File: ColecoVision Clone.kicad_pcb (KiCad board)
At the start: 2 copper layers, 149.4 x 99.1 mm, 141 parts, among them J1 Cartridge Slot, J2 Composite video, J3 PJ-102A, J4 RCJ-017, J5 Controller Port 1, J6 Controller Port 2, Q1 2n4401, Q2 Q_NJFET_GSD, Q3 2N3906, Q4 2N3904, Q5 2N3904, SW1 Power Toggle, SW2 Reset, U1 PLCCZ80, U10 SN76489AN, U11 74LS04, U12 74LS138 (Mem. Mapped), U13 74LS138 (I/O), U14 74LS02, U15 Controller 1, U16 Controller 2, U17 74LS05, U18 74LS05, U2 Work RAM, U20 74LS74, U22 74LS74, U23 74HCT00, U24 TPS60403DBVR, U3 BIOS ROM 27C256, U4 74HCT04, U5 TMS9918A, U6 74LS574, U7 74LS574, U8 74LS574, U9 VRAM, X1 14.31818MHz, Y1 10.738635MHZ

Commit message: U17 now powered
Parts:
- moved U17 0.06 mm to (93.6, 95.9)
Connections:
- U17 pad 14: (no net) -> VCC
- U17 pad 7: (no net) -> GND
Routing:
- net GND: track 1252.8 -> 1259.7 mm
- net VCC: track 926.4 -> 932.7 mm

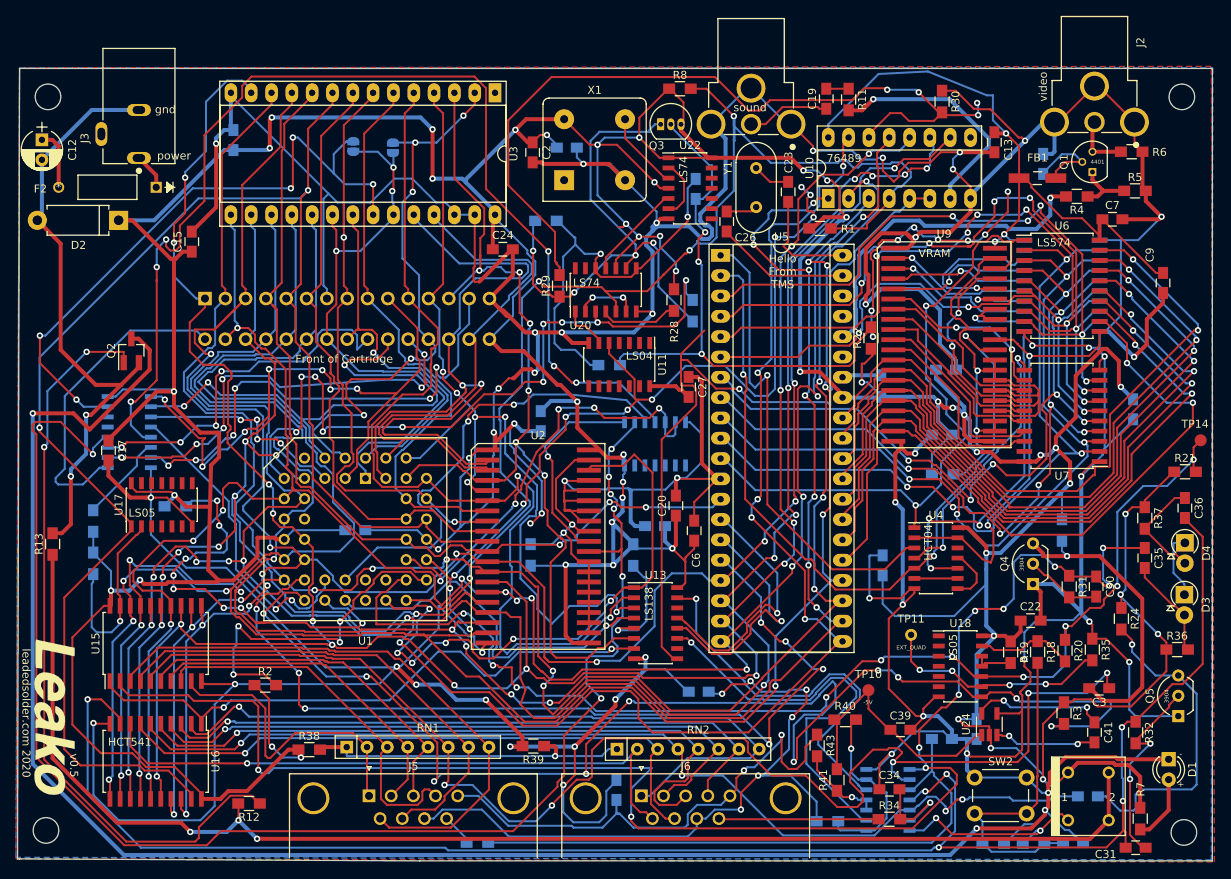
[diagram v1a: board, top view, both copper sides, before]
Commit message: Ground Vpp on the ROM
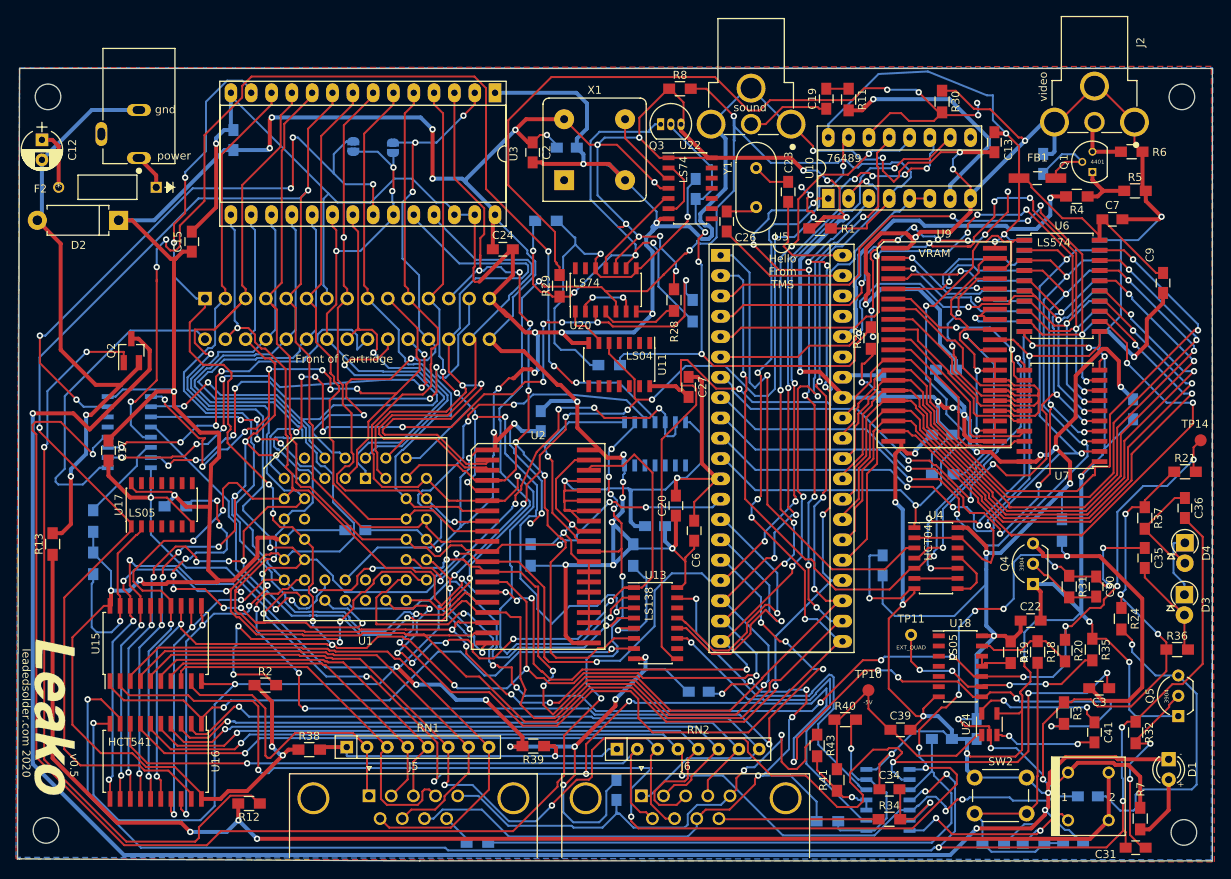
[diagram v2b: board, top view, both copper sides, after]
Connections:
- U3 pad 1: Net-(U3-Pad1) -> GND
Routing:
- net GND: track 1259.7 -> 1277.8 mm
- net CTRL_EN_1: track 51.7 -> 45.8 mm
- net Audio_WR: track 102.0 -> 97.0 mm
- net !INT: track 170.4 -> 166.4 mm
- net CTRL_EN_2: track 50.0 -> 46.2 mm
- net VCC: track 932.7 -> 929.1 mm
- net /Controllers/CTRL_PIN_8: track 86.4 -> 85.5 mm, vias 6 -> 5
- net !RESET: track 149.8 -> 149.2 mm

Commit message: Slowly clearing up vias
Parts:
- moved R30 5.61 mm to (185.8, 43.7), turned to 180 degrees
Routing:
- net GND: track 1277.8 -> 1211.7 mm, vias 55 -> 49
- net !M1: track 107.2 -> 52.6 mm, vias 11 -> 6
- net VCC: track 929.1 -> 907.6 mm
- net AUD_CLK: track 100.5 -> 83.6 mm, vias 4 -> 0
- net A7: track 119.7 -> 113.9 mm, vias 6 -> 4
- net !CART_0x80: track 46.1 -> 43.9 mm
- net /Video/VIDVCC: track 11.0 -> 9.73 mm
- net /Power/CLK_B: track 106.4 -> 105.5 mm, vias 11 -> 10
- net !WAIT: track 150.5 -> 149.8 mm
- net A13: track 76.5 -> 77.2 mm
- net !CART_0xA0: track 55.8 -> 55.3 mm
- net A12: vias 5 -> 4

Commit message: Purging vias
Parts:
- C25, R26: moved to F.Cu
- C34, C41, R32, R36: moved to B.Cu
- moved C25 7.78 mm to (159.3, 64.1), turned to 270 degrees
- moved C34 5.52 mm to (182.7, 126.2)
- moved R26 5.15 mm to (146.7, 61.3)
- moved TP11 5.13 mm to (191.6, 109.5)
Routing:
- net GND: track 1211.7 -> 1238.2 mm, vias 49 -> 48
- net Net-(C32-Pad1): track 129.4 -> 150.7 mm, vias 4 -> 3
- net VCC: track 907.6 -> 886.4 mm, vias 54 -> 49
- net !RD: track 59.0 -> 73.4 mm
- net !CPU_CLK: track 50.9 -> 39.1 mm, vias 2 -> 1
- net Net-(C34-Pad2): track 11.9 -> 19.3 mm
- net /Power/CLK_E: track 68.0 -> 60.9 mm, vias 4 -> 3
- net Net-(C3-Pad1): track 169.3 -> 162.3 mm
- net !WR: track 78.0 -> 74.5 mm
- net D0: track 282.7 -> 279.4 mm
- net Net-(C30-Pad1): track 192.9 -> 189.9 mm
- net A6: track 115.8 -> 112.9 mm
- net /Power/CLK_B: track 105.5 -> 102.8 mm, vias 10 -> 9
- net !WAIT: track 149.8 -> 152.4 mm
- net D6: track 290.3 -> 288.5 mm
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
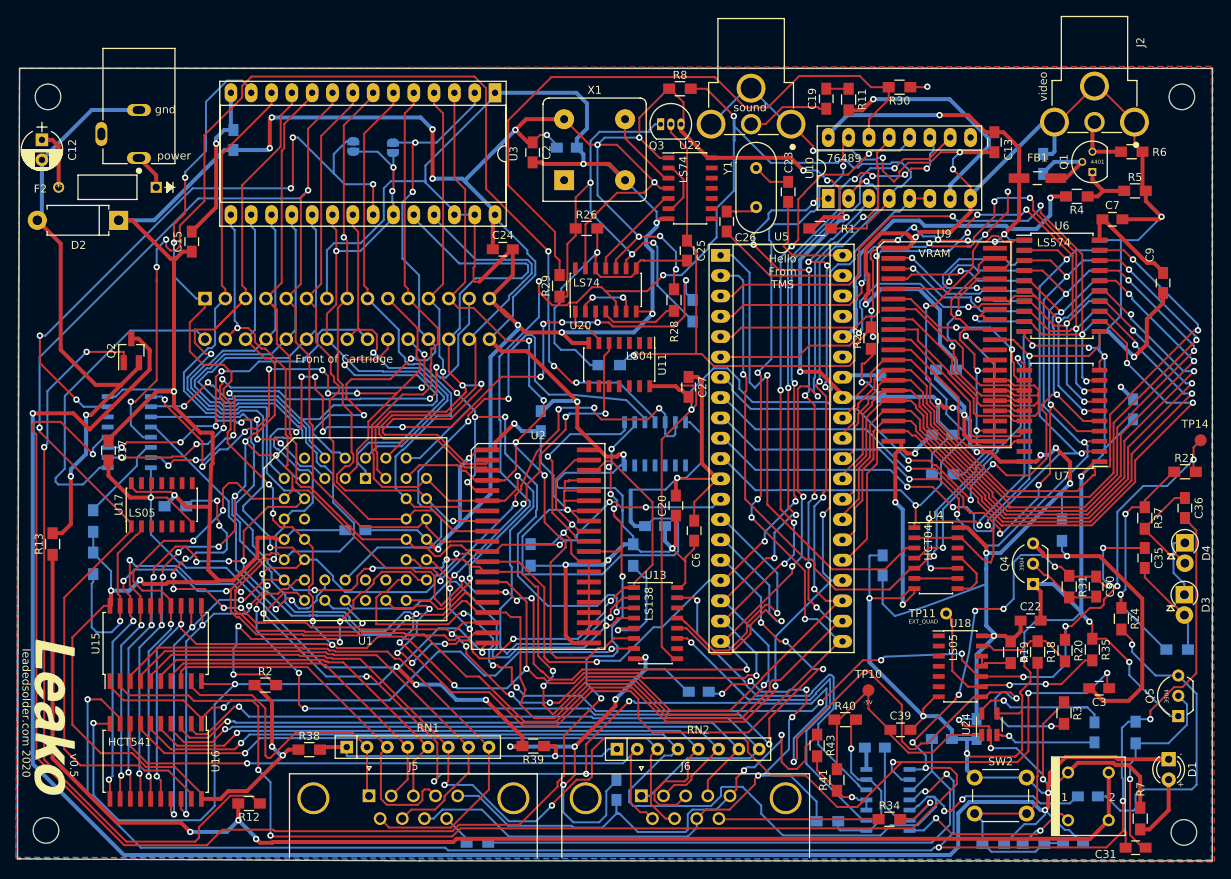
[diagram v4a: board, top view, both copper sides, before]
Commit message: Many fewer vias in the sound chip
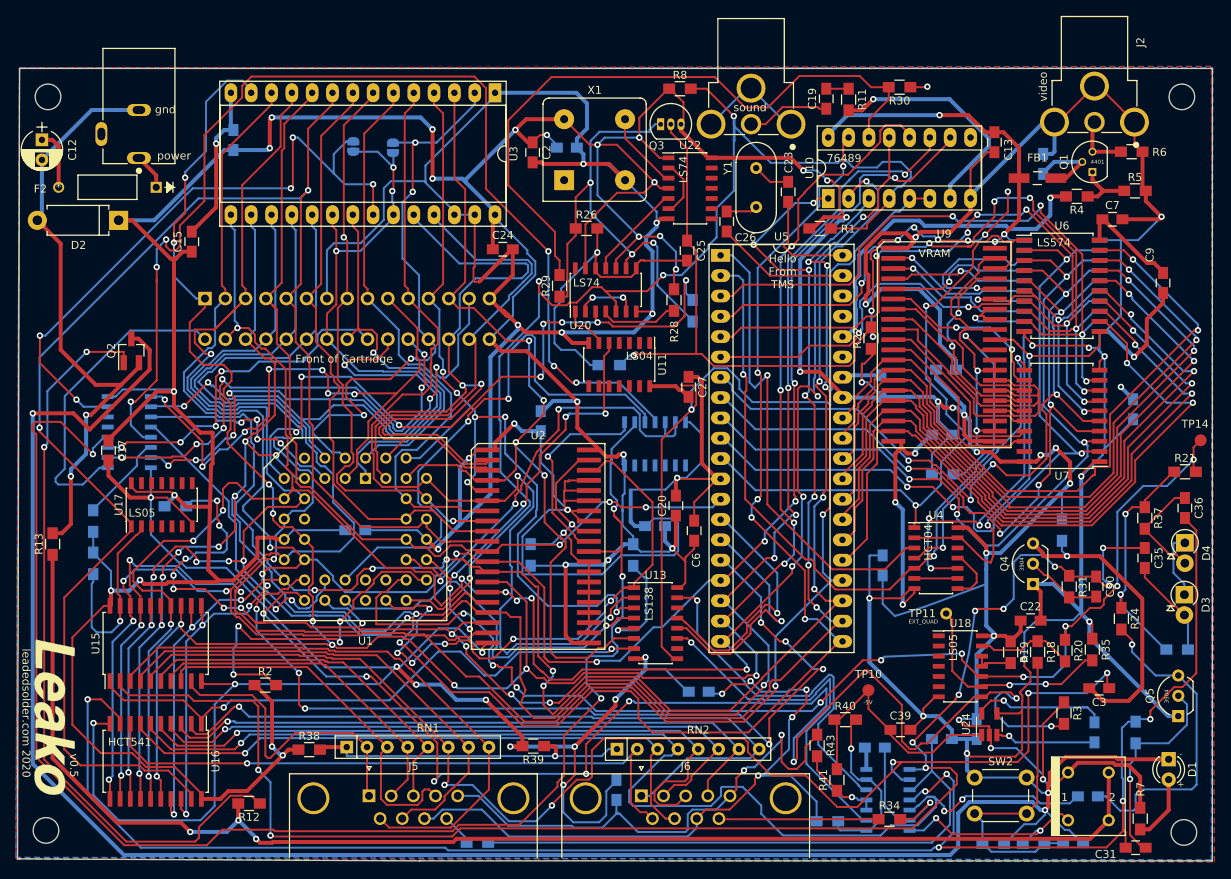
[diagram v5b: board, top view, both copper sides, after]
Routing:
- net GND: track 1238.2 -> 1209.7 mm, vias 48 -> 43
- net VCC: track 886.4 -> 871.7 mm
- net !CART_0xA0: track 55.3 -> 61.7 mm
- net !CART_0xE0: track 61.0 -> 65.6 mm
- net A14: track 67.6 -> 71.7 mm
- net CPU_CLK: track 90.1 -> 86.2 mm, vias 10 -> 8
- net D2: track 295.0 -> 297.5 mm, vias 16 -> 15
- net D4: track 297.2 -> 294.9 mm
- net D5: track 286.0 -> 284.8 mm
- net D0: track 279.4 -> 280.2 mm
- net !RD: track 73.4 -> 74.0 mm
- net A13: track 76.6 -> 76.1 mm
- net A0: track 116.2 -> 115.6 mm
- net D1: track 296.1 -> 295.7 mm, vias 16 -> 13
- net !RAM_CE: track 188.5 -> 188.8 mm, vias 7 -> 4
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
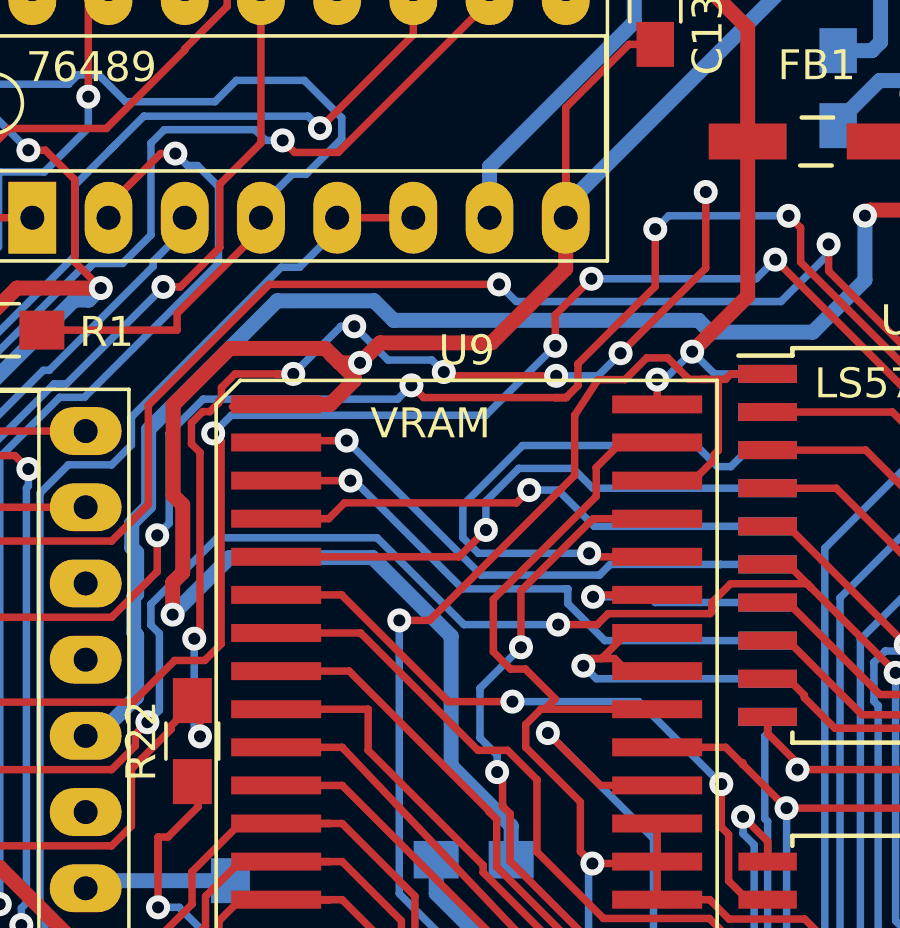
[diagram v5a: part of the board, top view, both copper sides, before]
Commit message: Under 500 vias now
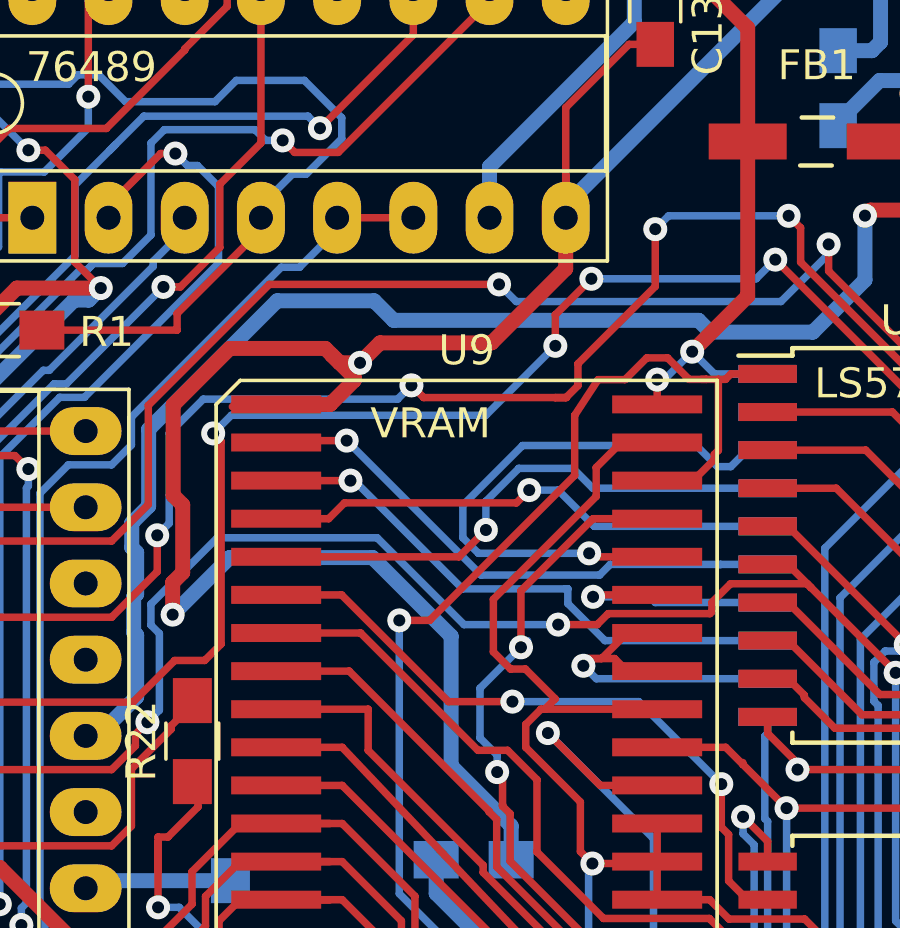
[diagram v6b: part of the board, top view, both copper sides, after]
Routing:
- net /Power/CLK_B: track 102.8 -> 66.8 mm, vias 9 -> 1
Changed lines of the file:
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@@
     (thickness 1.6)
     (drawings 38)
-    (tracks 5074)
+    (tracks 5038)
     (zones 0)
     (modules 141)
@@
   (segment (start 197.739 65.0875) (end 196.539 65.0875) (width 0.25) (layer F.Cu) (net 171) (status 30))
   (segment (start 192.278 70.31323) (end 192.278 72.066002) (width 0.25) (layer F.Cu) (net 171))
-  (segment (start 199.35825 56.73725) (end 199.39 56.769) (width 0.25) (layer F.Cu) (net 172))
-  (via (at 199.35825 56.73725) (size 0.8) (drill 0.4) (layers F.Cu B.Cu) (net 172))
-  (via (at 194.3735 62.865) (size 0.8) (drill 0.4) (layers F.Cu B.Cu) (net 172))
-  (segment (start 194.3735 62.865) (end 190.754 62.865) (width 0.25) (layer F.Cu) (net 172))
-  (via (at 190.627 62.738) (size 0.8) (drill 0.4) (layers F.Cu B.Cu) (net 172))
-  (segment (start 190.754 62.865) (end 190.627 62.738) (width 0.25) (layer F.Cu) (net 172))
   (segment (start 157.5435 48.6235) (end 157.5435 48.3235) (width 0.25) (layer B.Cu) (net 172) (status 30))
   (segment (start 157.226 48.6235) (end 157.226 48.3235) (width 0.25) (layer B.Cu) (net 172) (status 30))
-  (segment (start 190.627 62.738) (end 190.227001 62.338001) (width 0.25) (layer B.Cu) (net 172))
-  (segment (start 190.227001 62.338001) (end 188.766501 62.338001) (width 0.25) (layer B.Cu) (net 172))
-  (segment (start 188.766501 62.338001) (end 187.6425 61.214) (width 0.25) (layer B.Cu) (net 172))
-  (via (at 187.6425 61.214) (size 0.8) (drill 0.4) (layers F.Cu B.Cu) (net 172))
-  (segment (start 187.198 61.214) (end 187.6425 61.214) (width 0.25) (layer B.Cu) (net 172))
-  (segment (start 185.6105 62.8015) (end 187.198 61.214) (width 0.25) (layer B.Cu) (net 172))
-  (via (at 185.6105 62.8015) (size 0.8) (drill 0.4) (layers F.Cu B.Cu) (net 172))
-  (segment (start 185.069998 62.8015) (end 185.6105 62.8015) (width 0.25) (layer F.Cu) (net 172))
-  (segment (start 194.3735 62.865) (end 195.767676 62.865) (width 0.25) (layer B.Cu) (net 172))
-  (via (at 196.520627 62.112049) (size 0.8) (drill 0.4) (layers F.Cu B.Cu) (net 172))
-  (segment (start 195.767676 62.865) (end 196.520627 62.112049) (width 0.25) (layer B.Cu) (net 172))
-  (segment (start 199.35825 59.274426) (end 196.520627 62.112049) (width 0.25) (layer F.Cu) (net 172))
-  (segment (start 199.35825 56.73725) (end 199.35825 59.274426) (width 0.25) (layer F.Cu) (net 172))
   (segment (start 181.5355 74.533) (end 182.4355 73.633) (width 0.25) (layer F.Cu) (net 172) (status 20))
   (segment (start 180.21401 75.968904) (end 181.5355 74.647414) (width 0.25) (layer F.Cu) (net 172))
@@
   (segment (start 181.5355 74.647414) (end 181.5355 74.533) (width 0.25) (layer F.Cu) (net 172))
   (segment (start 182.4355 73.633) (end 182.4355 73.533) (width 0.25) (layer F.Cu) (net 172) (status 30))
-  (via (at 182.3085 71.628) (size 0.8) (drill 0.4) (layers F.Cu B.Cu) (net 172))
-  (segment (start 182.3085 74.692498) (end 182.499 74.882998) (width 0.25) (layer B.Cu) (net 172))
-  (via (at 182.499 74.882998) (size 0.8) (drill 0.4) (layers F.Cu B.Cu) (net 172))
-  (segment (start 182.3085 71.628) (end 182.3085 74.692498) (width 0.25) (layer B.Cu) (net 172))
   (segment (start 182.499 73.5965) (end 182.4355 73.533) (width 0.25) (layer F.Cu) (net 172) (status 30))
-  (segment (start 182.499 74.882998) (end 182.499 73.5965) (width 0.25) (layer F.Cu) (net 172) (status 20))
-  (segment (start 182.499 71.4375) (end 182.3085 71.628) (width 0.25) (layer F.Cu) (net 172))
-  (segment (start 183.128491 63.759509) (end 182.829192 64.058808) (width 0.25) (layer F.Cu) (net 172))
-  (segment (start 183.213999 63.257499) (end 183.213999 63.621089) (width 0.25) (layer F.Cu) (net 172))
-  (segment (start 182.499 65.4168) (end 182.499 71.4375) (width 0.25) (layer F.Cu) (net 172))
-  (segment (start 183.213999 63.621089) (end 183.128491 63.706597) (width 0.25) (layer F.Cu) (net 172))
-  (segment (start 182.21401 64.435808) (end 182.21401 65.13181) (width 0.25) (layer F.Cu) (net 172))
-  (segment (start 183.669998 62.8015) (end 183.213999 63.257499) (width 0.25) (layer F.Cu) (net 172))
-  (segment (start 182.829192 64.058808) (end 182.59101 64.058808) (width 0.25) (layer F.Cu) (net 172))
-  (segment (start 183.128491 63.706597) (end 183.128491 63.759509) (width 0.25) (layer F.Cu) (net 172))
-  (segment (start 182.21401 65.13181) (end 182.499 65.4168) (width 0.25) (layer F.Cu) (net 172))
-  (segment (start 182.59101 64.058808) (end 182.21401 64.435808) (width 0.25) (layer F.Cu) (net 172))
-  (segment (start 185.6105 62.8015) (end 183.669998 62.8015) (width 0.25) (layer F.Cu) (net 172))
   (via (at 152.5905 77.216) (size 0.8) (drill 0.4) (layers F.Cu B.Cu) (net 172))
   (segment (start 152.776501 77.029999) (end 152.5905 77.216) (width 0.25) (layer F.Cu) (net 172))
